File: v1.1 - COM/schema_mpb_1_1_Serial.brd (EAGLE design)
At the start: 89.8 x 49.5 mm, 64 parts, among them U1 MAX232PTH, U2 MAX232PTH, U3 MAX232PTH

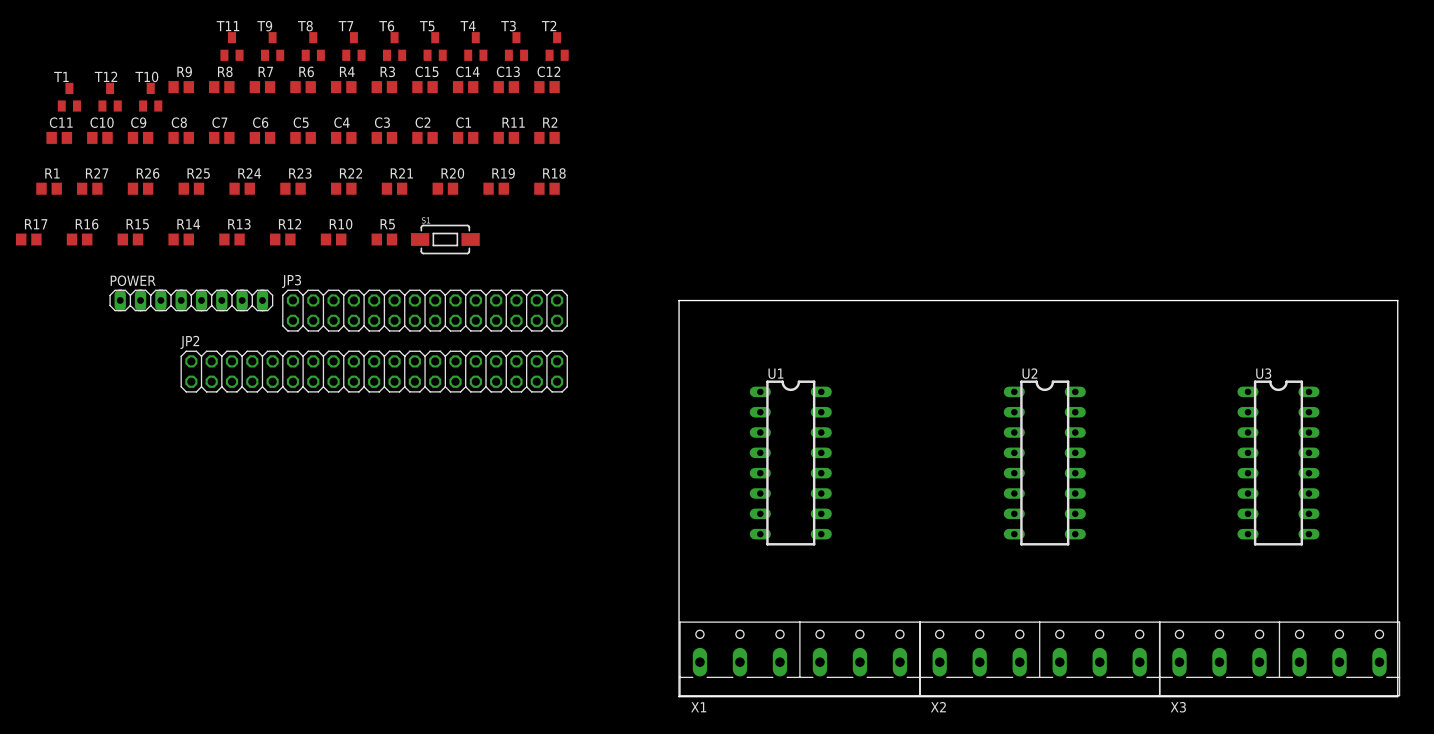
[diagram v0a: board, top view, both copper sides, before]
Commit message: RS232 Board
Routed tracks and added dimensions
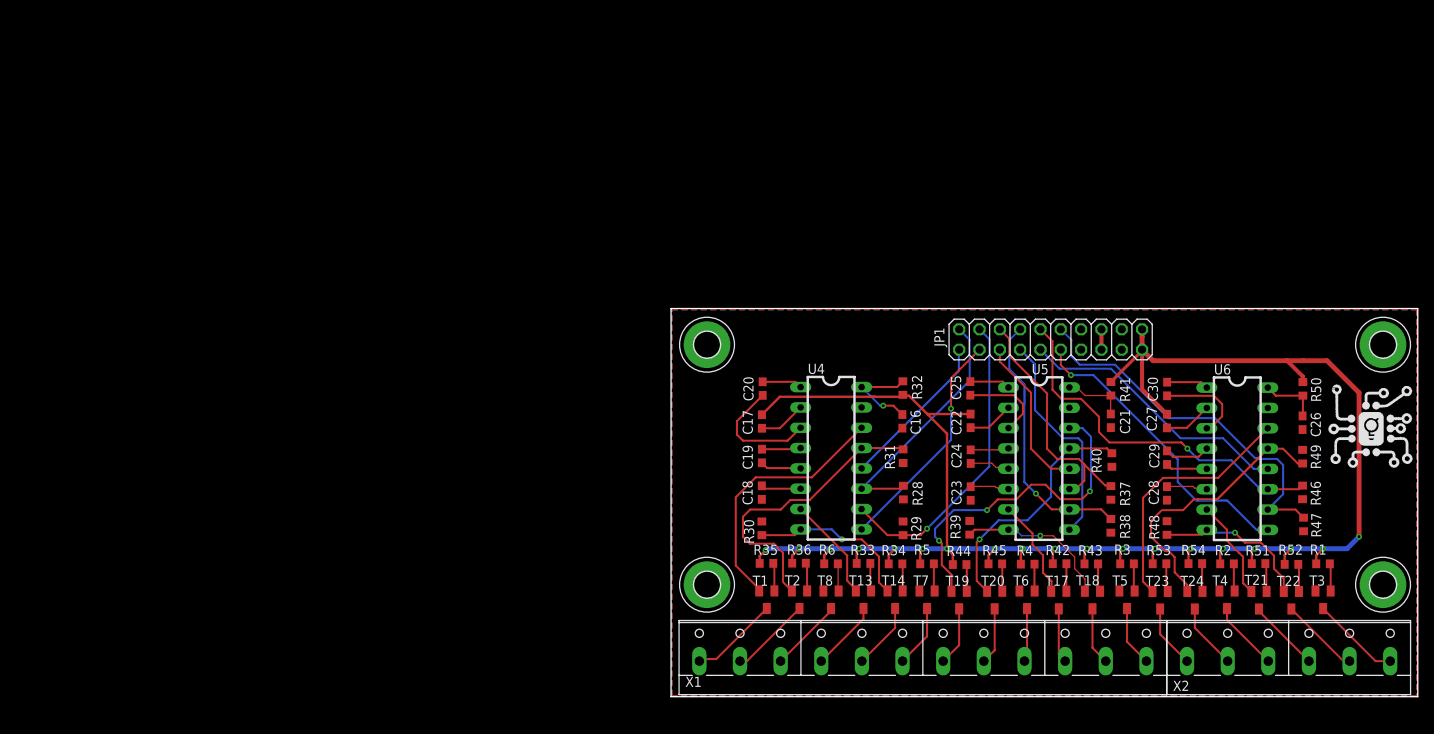
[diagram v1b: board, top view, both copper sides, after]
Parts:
- removed C1, C10, C11, C12, C13, C14, C15, C2, C3, C4, C5, C6, C7, C8, C9: .1uF, rcl:C0805
- removed JP2: (no value), pinhead:2X19
- removed JP3: (no value), pinhead:2X14
- removed POWER: 8x1F-H8.5, SmartPrj:1X08
- removed R10, R11, R19, R20: 10K, rcl:R0805
- removed R12, R13, R21, R22: 4k7, rcl:R0805
- removed R14, R23: 20R, rcl:R0805
- removed R15, R16, R17, R18, R24, R25, R26, R27, R7, R8, R9: 1k, rcl:R0805
- removed S1: SWITCH-MOMENTARY-2SMD-1101NE, SparkFun-Electromechanical:TACTILE-SWITCH-1101NE
- removed T10, T11, T12, T9: (no value), semicon-smd-ipc:SOT23
- removed U1, U2, U3: MAX232PTH, SparkFun-DigitalIC:DIL16
- removed X3: (no value), con-wago-500:W237-6
- added C16, C17, C18, C19, C20, C21, C22, C23, C24, C25, C26, C27, C28, C29, C30: .1uF, rcl:C0603
- added H1, H2, H3, H4: MOUNT-PAD-ROUND3.2, holes:3,2-PAD
- added JP1: (no value), pinhead:2X10
- added R28, R29, R37, R38, R46, R47: 10K, rcl:R0603
- added R30, R31, R39, R40, R48, R49: 4k7, rcl:R0603
- added R32, R41, R50: 20R, rcl:R0603
- added R33, R34, R35, R36, R42, R43, R44, R45, R51, R52, R53, R54: 1k, rcl:R0603
- added T13, T14, T17, T18, T19, T20, T21, T22, T23, T24: (no value), semicon-smd-ipc:SOT23
- added U4, U5, U6: MAX232PTH, SparkFun-DigitalIC:DIL16
- R1, R2: value 10K -> 1k; device rcl:R0805 -> rcl:R0603
- R3, R4: value 4k7 -> 1k; device rcl:R0805 -> rcl:R0603
- R5: value 20R -> 1k; device rcl:R0805 -> rcl:R0603
- R6: device rcl:R0805 -> rcl:R0603
- X1: device con-wago-500:W237-6 -> con-wago-508:W237-12P
- X2: device con-wago-500:W237-6 -> con-wago-508:W237-6P
- moved R1 166.0 mm to (80.5, 16.6)
- moved T3 122.3 mm to (80.5, 12.1), turned to 180 degrees
- moved T4 116.6 mm to (68.5, 12.1), turned to 180 degrees
- moved T5 110.7 mm to (56.0, 12.1), turned to 180 degrees
- moved R3 110.3 mm to (56.0, 16.6)
- moved T1 107.4 mm to (11.0, 12.1), turned to 180 degrees
- moved T6 105.0 mm to (43.5, 12.1), turned to 180 degrees
- moved R4 104.2 mm to (43.6, 16.6)
- moved R2 100.3 mm to (68.5, 16.6)
- moved T7 99.6 mm to (31.0, 12.1), turned to 180 degrees
- moved T8 94.7 mm to (19.0, 12.1), turned to 180 degrees
- moved R6 88.9 mm to (19.0, 16.6)
- moved R5 79.0 mm to (31.0, 16.6)
- moved T2 75.5 mm to (15.1, 12.1), turned to 180 degrees
- moved X2 31.1 mm to (76.2, 5.08)
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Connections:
- removed net +12V: POWER.1
- removed net 3.3V: C12.2, C3.2, C7.2, POWER.4, R14.2, R15.1, R16.1, R17.1, R18.1, R23.2, R24.1, R25.1, R26.1, R27.1, R5.2, R6.1, R7.1, R8.1, R9.1, X1.6, X2.6, X3.6
- removed net ADC0: JP2.1
- removed net ADC1: JP2.3
- removed net ADC12: JP2.25
- removed net ADC13: JP2.27
- removed net ADC14: JP2.29
- removed net ADC15: JP2.31
- removed net ADC2: JP2.5
- removed net ADC3: JP2.7
- removed net ADC4: JP2.9
- removed net ADC5: JP2.11
- removed net ADC6: JP2.13
- removed net ADC7: JP2.15
- removed net IO0: JP2.4
- removed net IO1: JP2.6
- removed net IO2: JP2.10
- removed net IO3: JP2.12
- removed net IO4: JP2.2
- removed net IO5: JP2.8
- removed net IO6: JP2.18
- removed net IO7: JP2.20
- removed net IO8: JP2.22
- removed net IO9: JP2.24
- removed net N$10: R17.2, T7.1
- removed net N$11: R18.2, T8.1
- removed net N$12: C15.2, U3.3
- removed net N$13: C15.1, U3.1
- removed net N$14: C14.2, U3.5
- removed net N$15: C6.2, U1.3
- removed net N$16: C6.1, U1.1
- removed net N$17: C5.2, U1.5
- removed net N$18: C5.1, U1.4
- removed net N$19: C4.1, U1.6
- removed net N$20: C2.2, R5.1, U1.16
- removed net N$21: C3.1, U1.2
- removed net N$22: R6.2, T1.1
- removed net N$23: R7.2, T2.1
- removed net N$24: R8.2, T3.1
- removed net N$25: R9.2, T4.1
- removed net N$26: C14.1, U3.4
- removed net N$27: C13.1, U3.6
- removed net N$28: C11.2, R23.1, U3.16
- removed net N$29: C12.1, U3.2
- removed net N$30: R24.2, T9.1
- removed net N$31: R25.2, T10.1
- removed net N$32: R26.2, T11.1
- removed net N$33: R27.2, T12.1
- removed net N$7: C7.1, U2.2
- removed net N$8: R15.2, T5.1
- removed net N$9: R16.2, T6.1
- removed net PA0: JP2.33
- removed net PA1: JP2.35
- removed net PA2: JP2.37
- removed net PA3: JP3.28
- removed net PA4: JP3.26
- removed net PA5: JP3.24
- removed net PA6: JP3.22
- removed net PA7: JP3.20
- removed net PB0: JP2.26
- removed net PB1: JP2.28
- removed net PB2: JP2.30
- removed net PB3: JP2.32
- removed net PB4: JP2.34
- removed net PB5: JP2.36
- removed net PB6: JP2.38
- removed net PB7: JP3.27
- removed net PC0: JP3.3
- removed net PC1: JP3.1
- removed net PC2: JP3.2
- removed net PC3: JP3.4
- removed net PC4: JP3.6
- removed net PC5: JP3.8
- removed net PC6: JP3.10
- removed net PC7: JP3.12
- removed net PD7: JP3.9
- removed net PG0: JP3.7
- removed net PG1: JP3.5
- removed net PG2: JP3.18
- removed net PL2: JP3.25
- removed net PL3: JP3.23
- removed net PL4: JP3.21
- removed net PL5: JP3.19
- removed net R1IN_1: R4.2, T4.2, U1.13
- removed net R1IN_1#: T4.3, X1.2
- removed net R1IN_2: R13.2, T8.2, U2.13
- removed net R1IN_2#: T8.3, X2.2
- removed net R1IN_3: R22.2, T12.2, U3.13
- removed net R1IN_3#: T12.3, X3.2
- removed net R2IN_1: R3.2, T2.2, U1.8
- removed net R2IN_1#: T2.3, X1.3
- removed net R2IN_2: R12.2, T6.2, U2.8
- removed net R2IN_2#: T6.3, X2.3
- removed net R2IN_3: R21.2, T10.2, U3.8
- removed net R2IN_3#: T10.3, X3.3
- removed net R2OUT_3: U3.9
- removed net REG_5V: POWER.2, POWER.5
- removed net RESET: POWER.3, S1.1
- removed net SCL: JP3.17
- removed net SDA: JP3.15
- removed net T1OUT_1: T3.2, U1.14
- removed net T1OUT_1#: T3.3, X1.4
- removed net T1OUT_2: T7.2, U2.14
- removed net T1OUT_2#: T7.3, X2.4
- removed net T1OUT_3: T11.2, U3.14
- removed net T1OUT_3#: T11.3, X3.4
- removed net T2IN_3: R20.2, U3.10
- removed net T2OUT_1: T1.2, U1.7
- removed net T2OUT_1#: T1.3, X1.5
- removed net T2OUT_2: T5.2, U2.7
- removed net T2OUT_2#: T5.3, X2.5
- removed net T2OUT_3: T9.2, U3.7
- removed net T2OUT_3#: T9.3, X3.5
- removed net VIN: POWER.8
- new net +3V3: C17.2, C22.2, C27.2, JP1.19, JP1.20, R1.1, R2.1, R3.1, R32.2, R33.1, R34.1, R35.1, R36.1, R4.1, R41.2, R42.1, R43.1, R44.1, R45.1, R5.1, R50.2, R51.1, R52.1, R53.1, R54.1, R6.1
- new net +5V: JP1.15, JP1.16
- new net GND1: T8.3, X1.3
- new net GND2: T7.3, X1.6
- new net GND3: T6.3, X1.9
- new net GND4: T5.3, X1.12
- new net GND5: T4.3, X2.3
- new net GND6: T3.3, X2.6
- new net N$34: C20.2, U4.3
- new net N$35: C20.1, U4.1
- new net N$36: C19.2, U4.5
- new net N$37: C19.1, U4.4
- new net N$38: C18.1, U4.6
- new net N$39: C16.2, R32.1, U4.16
- new net N$40: C17.1, U4.2
- new net N$41: R33.2, T13.1
- new net N$42: R34.2, T14.1
- new net N$43: R35.2, T1.1
- new net N$44: R36.2, T2.1
- new net N$45: C25.2, U5.3
- new net N$46: C25.1, U5.1
- new net N$47: C24.2, U5.5
- new net N$48: C24.1, U5.4
- new net N$49: C23.1, U5.6
- new net N$50: C21.2, R41.1, U5.16
- new net N$51: C22.1, U5.2
- new net N$52: R42.2, T17.1
- new net N$53: R43.2, T18.1
- new net N$54: R44.2, T19.1
- new net N$55: R45.2, T20.1
- new net N$56: C30.2, U6.3
- new net N$57: C30.1, U6.1
- new net N$58: C29.2, U6.5
- new net N$59: C29.1, U6.4
- new net N$60: C28.1, U6.6
- new net N$61: C26.2, R50.1, U6.16
- new net N$62: C27.1, U6.2
- new net N$63: R51.2, T21.1
- new net N$64: R52.2, T22.1
- new net N$65: R53.2, T23.1
- new net N$66: R54.2, T24.1
- new net RX1: JP1.1, U4.12
- new net RX2: JP1.3, U4.9
- new net RX3: JP1.5, U5.12
- new net RX4: JP1.7, U5.9
- new net RX5: JP1.9, U6.12
- new net RX6: JP1.11, U6.9
- new net RXD1#: T2.3, X1.2
- new net RXD2#: T14.3, X1.5
- new net RXD3#: T20.3, X1.8
- new net RXD4#: T18.3, X1.11
- new net RXD5#: T24.3, X2.2
- new net RXD6: R48.2, T22.2, U6.8
- new net RXD6#: T22.3, X2.5
- new net TX1: JP1.2, R28.2, U4.11
- new net TX2: JP1.4, R29.2, U4.10
- new net TX3: JP1.6, R37.2, U5.11
- new net TX4: JP1.8, R38.2, U5.10
- new net TX5: JP1.10, R46.2, U6.11
- new net TX6: JP1.12, R47.2, U6.10
- new net TXD1#: T1.3, X1.1
- new net TXD2#: T13.3, X1.4
- new net TXD3#: T19.3, X1.7
- new net TXD4#: T17.3, X1.10
- new net TXD5#: T23.3, X2.1
- new net TXD6: T21.2, U6.7
- new net TXD6#: T21.3, X2.4
- net GND: now also C16.1, C18.2, C21.1, C23.2, C26.1, C28.2, JP1.13, JP1.14, JP1.17, JP1.18, R28.1, R29.1, R30.1, R31.1, R37.1, R38.1, R39.1, R40.1, R46.1, R47.1, R48.1, R49.1, T3.2, T4.2, T5.2, T6.2, T7.2, T8.2, U4.15, U5.15, U6.15; no longer C1.1, C11.1, C13.2, C2.1, C4.2, C8.2, POWER.6, POWER.7, R1.1, R10.1, R11.1, R12.1, R13.1, R19.1, R2.1, R20.1, R21.1, R22.1, R3.1, R4.1, S1.2, U1.15, U2.15, U3.15, X1.1, X2.1, X3.1
- net N$1: now also R1.2, T3.1; no longer C10.2, U2.3
- net N$2: now also R2.2, T4.1; no longer C10.1, U2.1
- net N$3: now also R3.2, T5.1; no longer C9.2, U2.5
- net N$4: now also R4.2, T6.1; no longer C9.1, U2.4
- net N$5: now also R5.2, T7.1; no longer C8.1, U2.6
- net N$6: now also R6.2, T8.1; no longer C1.2, R14.1, U2.16
- net RXD1: now also R31.2, T2.2, U4.13; no longer JP3.13, U1.12
- net RXD2: now also R30.2, T14.2, U4.8; no longer JP2.14, U1.9
- net RXD3: now also R40.2, T20.2, U5.13; no longer JP3.14, U2.12
- net RXD4: now also R39.2, T18.2, U5.8; no longer JP2.19, U2.9
- net RXD5: now also R49.2, T24.2, U6.13; no longer JP2.23, U3.12
- net TXD1: now also T1.2, U4.14; no longer JP3.11, R1.2, U1.11
- net TXD2: now also T13.2, U4.7; no longer JP2.16, R2.2, U1.10
- net TXD3: now also T19.2, U5.14; no longer JP3.16, R10.2, U2.11
- net TXD4: now also T17.2, U5.7; no longer JP2.17, R11.2, U2.10
- net TXD5: now also T23.2, U6.14; no longer JP2.21, R19.2, U3.11
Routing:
- net +3V3: track 0.00 -> 238.2 mm, vias 0 -> 19
- net TX6: track 0.00 -> 47.3 mm
- net RXD5: track 0.00 -> 46.9 mm
- net TX5: track 0.00 -> 45.9 mm, vias 0 -> 1
- net TXD3: track 0.00 -> 41.5 mm, vias 0 -> 3
- net TX2: track 0.00 -> 38.5 mm, vias 0 -> 1
- net TX4: track 0.00 -> 38.4 mm, vias 0 -> 1
- net RX6: track 0.00 -> 38.0 mm, vias 0 -> 1
- net RXD1: track 0.00 -> 37.2 mm
- net RX5: track 0.00 -> 34.6 mm
- net TXD1: track 0.00 -> 32.2 mm
- net TX3: track 0.00 -> 31.8 mm
- net TX1: track 0.00 -> 31.4 mm
- net TXD5: track 0.00 -> 31.4 mm
- net RXD3: track 0.00 -> 30.9 mm, vias 0 -> 1
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- added copper zone on layer 1, net GND
- added copper zone on layer 16, net GND
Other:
- board size 89.8 x 49.5 mm -> 93.3 x 48.5 mm
